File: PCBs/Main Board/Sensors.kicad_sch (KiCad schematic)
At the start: 3 parts, among them J6 436500301, J7 436500301, J8 43650-0401

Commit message: Remove steppers, add OLED
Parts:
- renumbered J6 to J7, J7 to J8, J8 to J9
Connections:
- net pH_rx renamed SCL
- net pH_tx renamed SDA
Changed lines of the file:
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@@
     )
   )
-  (global_label "pH_tx" (shape input) (at 135.89 76.2 0) (fields_autoplaced)
+  (global_label "SDA" (shape input) (at 135.89 76.2 0) (fields_autoplaced)
     (effects (font (size 1.27 1.27)) (justify left))
-    (property "Intersheet References" "${INTERSHEET_REFS}" (id 0) (at 143.5041 76.1206 0)
+    (property "Intersheet References" "${INTERSHEET_REFS}" (id 0) (at 141.8712 76.1206 0)
       (effects (font (size 1.27 1.27)) (justify left) hide)
     )
@@
     )
   )
-  (global_label "pH_rx" (shape input) (at 135.89 80.01 0) (fields_autoplaced)
+  (global_label "SCL" (shape input) (at 135.89 80.01 0) (fields_autoplaced)
     (effects (font (size 1.27 1.27)) (justify left))
-    (property "Intersheet References" "${INTERSHEET_REFS}" (id 0) (at 143.5645 79.9306 0)
+    (property "Intersheet References" "${INTERSHEET_REFS}" (id 0) (at 141.8107 79.9306 0)
       (effects (font (size 1.27 1.27)) (justify left) hide)
     )
@@
   (symbol (lib_id "power:GND") (at 133.35 62.23 0) (unit 1)
     (in_bom yes) (on_board yes) (fields_autoplaced)
-    (property "Reference" "#PWR011" (id 0) (at 133.35 68.58 0)
+    (property "Reference" "#PWR019" (id 0) (at 133.35 68.58 0)
       (effects (font (size 1.27 1.27)) hide)
     )
@@
   (symbol (lib_id "power:GND") (at 104.14 67.31 0) (unit 1)
     (in_bom yes) (on_board yes) (fields_autoplaced)
-    (property "Reference" "#PWR010" (id 0) (at 104.14 73.66 0)
+    (property "Reference" "#PWR018" (id 0) (at 104.14 73.66 0)
       (effects (font (size 1.27 1.27)) hide)
     )
@@
   (symbol (lib_id "power:GND") (at 55.88 90.17 0) (unit 1)
     (in_bom yes) (on_board yes) (fields_autoplaced)
-    (property "Reference" "#PWR09" (id 0) (at 55.88 96.52 0)
+    (property "Reference" "#PWR017" (id 0) (at 55.88 96.52 0)
       (effects (font (size 1.27 1.27)) hide)
     )
@@
   (symbol (lib_id "43650-0401:43650-0401") (at 130.81 52.07 90) (unit 1)
     (in_bom yes) (on_board yes) (fields_autoplaced)
-    (property "Reference" "J8" (id 0) (at 139.7 50.7999 90)
+    (property "Reference" "J9" (id 0) (at 139.7 50.7999 90)
       (effects (font (size 1.27 1.27)) (justify right))
     )
@@
   (symbol (lib_id "436500301:436500301") (at 73.66 54.61 90) (unit 1)
     (in_bom yes) (on_board yes) (fields_autoplaced)
-    (property "Reference" "J6" (id 0) (at 80.01 49.5299 90)
+    (property "Reference" "J7" (id 0) (at 80.01 49.5299 90)
       (effects (font (size 1.27 1.27)) (justify right))
     )
@@
   (symbol (lib_id "436500301:436500301") (at 101.6 54.61 90) (unit 1)
     (in_bom yes) (on_board yes) (fields_autoplaced)
-    (property "Reference" "J7" (id 0) (at 107.95 49.5299 90)
+    (property "Reference" "J8" (id 0) (at 107.95 49.5299 90)
       (effects (font (size 1.27 1.27)) (justify right))
     )

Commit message: Changed some pins
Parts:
- added J11: 436500301, SnapEDA Library:MOLEX_436500301, symbol 436500301:436500301
- renumbered J9 to J10, J7 to J8, J8 to J9
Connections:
- net 3V3: now also J11.1
- new net waterLevel: J11.3
- no-connect marks 0 -> 1
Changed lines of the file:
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@@
 (kicad_sch (version 20211123) (generator eeschema)
   (paper "A4")
+  (no_connect (at 162.56 59.69))
   (wire (pts (xy 128.27 80.01) (xy 135.89 80.01))
     (stroke (width 0) (type default) (color 0 0 0 0))
@@
     (stroke (width 0) (type default) (color 0 0 0 0))
   )
+  (wire (pts (xy 165.1 62.23) (xy 165.1 59.69))
+    (stroke (width 0) (type default) (color 0 0 0 0))
+  )
   (wire (pts (xy 73.66 59.69) (xy 73.66 85.09))
     (stroke (width 0) (type default) (color 0 0 0 0))
@@
     (stroke (width 0) (type default) (color 0 0 0 0))
   )
+  (wire (pts (xy 160.02 66.04) (xy 160.02 59.69))
+    (stroke (width 0) (type default) (color 0 0 0 0))
+  )
   (wire (pts (xy 130.81 62.23) (xy 130.81 76.2))
     (stroke (width 0) (type default) (color 0 0 0 0))
@@
     (stroke (width 0) (type default) (color 0 0 0 0))
   )
+  (global_label "waterLevel" (shape input) (at 165.1 62.23 0) (fields_autoplaced)
+    (effects (font (size 1.27 1.27)) (justify left))
+    (property "Intersheet References" "${INTERSHEET_REFS}" (id 0) (at 177.4312 62.1506 0)
+      (effects (font (size 1.27 1.27)) (justify left) hide)
+    )
+  )
+  (global_label "3V3" (shape input) (at 160.02 66.04 0) (fields_autoplaced)
+    (effects (font (size 1.27 1.27)) (justify left))
+    (property "Intersheet References" "${INTERSHEET_REFS}" (id 0) (at 165.9407 65.9606 0)
+      (effects (font (size 1.27 1.27)) (justify left) hide)
+    )
+  )
   (global_label "ec_A" (shape input) (at 55.88 80.01 180) (fields_autoplaced)
     (effects (font (size 1.27 1.27)) (justify right))
@@
   (symbol (lib_id "power:GND") (at 133.35 62.23 0) (unit 1)
     (in_bom yes) (on_board yes) (fields_autoplaced)
-    (property "Reference" "#PWR019" (id 0) (at 133.35 68.58 0)
+    (property "Reference" "#PWR022" (id 0) (at 133.35 68.58 0)
       (effects (font (size 1.27 1.27)) hide)
     )
@@
   (symbol (lib_id "power:GND") (at 104.14 67.31 0) (unit 1)
     (in_bom yes) (on_board yes) (fields_autoplaced)
-    (property "Reference" "#PWR018" (id 0) (at 104.14 73.66 0)
+    (property "Reference" "#PWR021" (id 0) (at 104.14 73.66 0)
       (effects (font (size 1.27 1.27)) hide)
     )
@@
     (pin "1")
   )
+  (symbol (lib_id "436500301:436500301") (at 162.56 54.61 90) (unit 1)
+    (in_bom yes) (on_board yes) (fields_autoplaced)
+    (property "Reference" "J11" (id 0) (at 168.91 49.5299 90)
+      (effects (font (size 1.27 1.27)) (justify right))
+    )
+    (property "Value" "436500301" (id 1) (at 168.91 52.0699 90)
+      (effects (font (size 1.27 1.27)) (justify right))
+    )
+    (property "Footprint" "SnapEDA Library:MOLEX_436500301" (id 2) (at 162.56 54.61 0)
+      (effects (font (size 1.27 1.27)) (justify left bottom) hide)
+    )
+    (property "Datasheet" "" (id 3) (at 162.56 54.61 0)
+      (effects (font (size 1.27 1.27)) (justify left bottom) hide)
+    )
+    (property "MAXIMUM_PACKAGE_HEIGHT" "5.57 mm" (id 4) (at 162.56 54.61 0)
+      (effects (font (size 1.27 1.27)) (justify left bottom) hide)
+    )
+    (property "PARTREV" "D7" (id 5) (at 162.56 54.61 0)
+      (effects (font (size 1.27 1.27)) (justify left bottom) hide)
+    )
+    (property "MANUFACTURER" "Molex" (id 6) (at 162.56 54.61 0)
+      (effects (font (size 1.27 1.27)) (justify left bottom) hide)
+    )
+    (property "STANDARD" "Manufacturer Recommendations" (id 7) (at 162.56 54.61 0)
+      (effects (font (size 1.27 1.27)) (justify left bottom) hide)
+    )
+    (pin "1")
+    (pin "2")
+    (pin "3")
+  )
   (symbol (lib_id "power:GND") (at 55.88 90.17 0) (unit 1)
     (in_bom yes) (on_board yes) (fields_autoplaced)
-    (property "Reference" "#PWR017" (id 0) (at 55.88 96.52 0)
+    (property "Reference" "#PWR020" (id 0) (at 55.88 96.52 0)
       (effects (font (size 1.27 1.27)) hide)
     )
@@
   (symbol (lib_id "43650-0401:43650-0401") (at 130.81 52.07 90) (unit 1)
     (in_bom yes) (on_board yes) (fields_autoplaced)
-    (property "Reference" "J9" (id 0) (at 139.7 50.7999 90)
+    (property "Reference" "J10" (id 0) (at 139.7 50.7999 90)
       (effects (font (size 1.27 1.27)) (justify right))
     )
@@
   (symbol (lib_id "436500301:436500301") (at 73.66 54.61 90) (unit 1)
     (in_bom yes) (on_board yes) (fields_autoplaced)
-    (property "Reference" "J7" (id 0) (at 80.01 49.5299 90)
+    (property "Reference" "J8" (id 0) (at 80.01 49.5299 90)
       (effects (font (size 1.27 1.27)) (justify right))
     )
@@
   (symbol (lib_id "436500301:436500301") (at 101.6 54.61 90) (unit 1)
     (in_bom yes) (on_board yes) (fields_autoplaced)
-    (property "Reference" "J8" (id 0) (at 107.95 49.5299 90)
-      (effects (font (size 1.27 1.27)) (justify right))
-    )
+    (property "Reference" "J9" (id 0) (at 107.95 49.5299 90)
+      (effects (font (size 1.27 1.27)) (justify right))
+    )

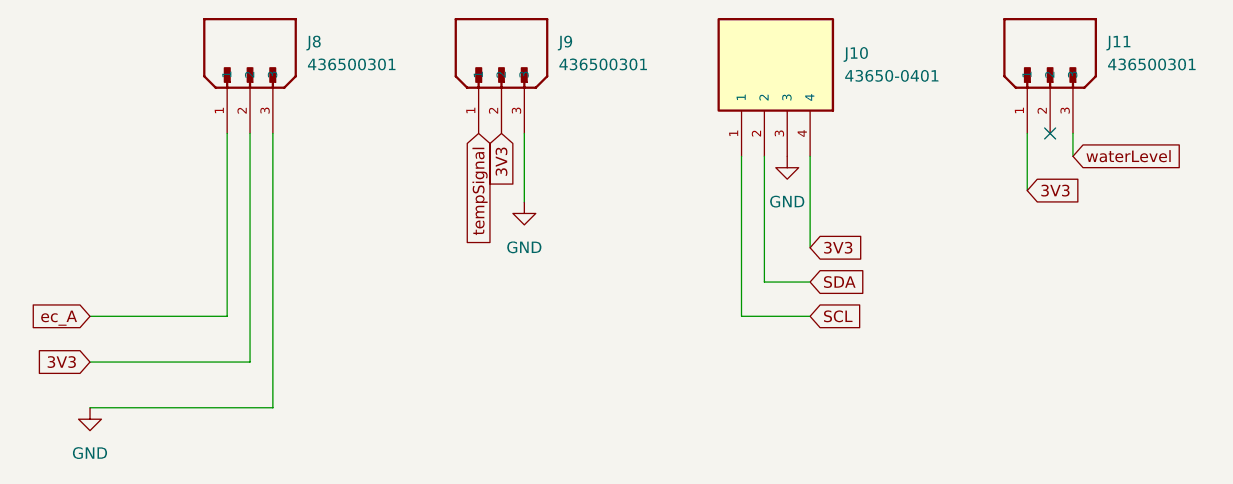
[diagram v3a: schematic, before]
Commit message: Changes to PCB, wired sensors to board
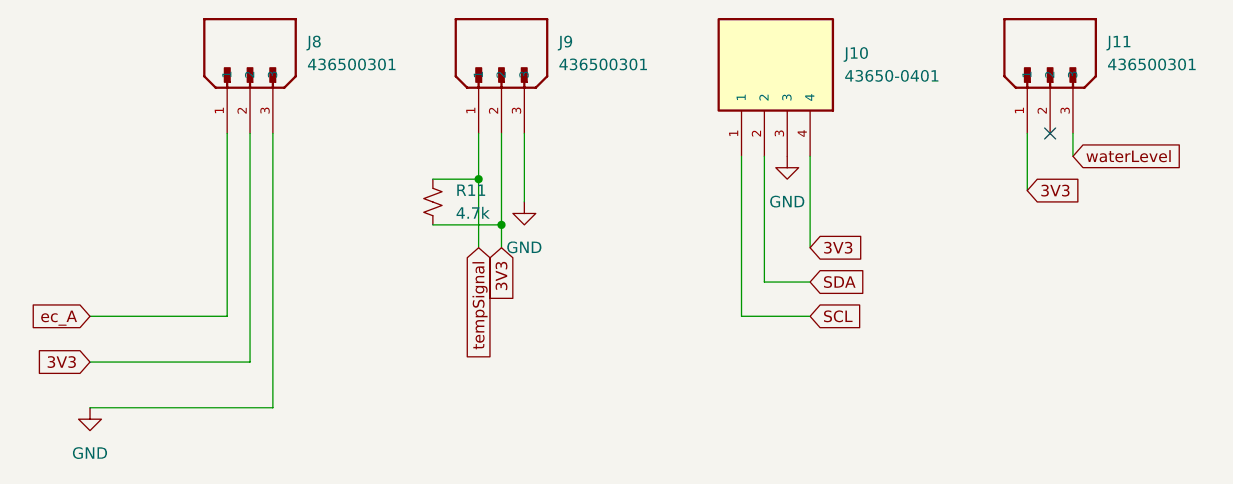
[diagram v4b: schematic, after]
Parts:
- added R11: 4.7k, Resistor_THT:R_Axial_DIN0204_L3.6mm_D1.6mm_P7.62mm_Horizontal, symbol Device:R_Small_US
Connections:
- net 3V3: now also R11.2
- net tempSignal: now also R11.1
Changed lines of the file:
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@@
 (kicad_sch (version 20211123) (generator eeschema)
   (paper "A4")
+  (junction (at 101.6 69.85) (diameter 0) (color 0 0 0 0)
+  )
+  (junction (at 99.06 64.77) (diameter 0) (color 0 0 0 0)
+  )
   (no_connect (at 162.56 59.69))
   (wire (pts (xy 128.27 80.01) (xy 135.89 80.01))
@@
   )
   (wire (pts (xy 55.88 85.09) (xy 73.66 85.09))
+    (stroke (width 0) (type default) (color 0 0 0 0))
+  )
+  (wire (pts (xy 93.98 64.77) (xy 99.06 64.77))
     (stroke (width 0) (type default) (color 0 0 0 0))
   )
@@
     (stroke (width 0) (type default) (color 0 0 0 0))
   )
+  (wire (pts (xy 99.06 72.39) (xy 99.06 64.77))
+    (stroke (width 0) (type default) (color 0 0 0 0))
+  )
+  (wire (pts (xy 93.98 69.85) (xy 101.6 69.85))
+    (stroke (width 0) (type default) (color 0 0 0 0))
+  )
   (wire (pts (xy 130.81 62.23) (xy 130.81 76.2))
+    (stroke (width 0) (type default) (color 0 0 0 0))
+  )
+  (wire (pts (xy 99.06 64.77) (xy 99.06 59.69))
+    (stroke (width 0) (type default) (color 0 0 0 0))
+  )
+  (wire (pts (xy 101.6 72.39) (xy 101.6 69.85))
+    (stroke (width 0) (type default) (color 0 0 0 0))
+  )
+  (wire (pts (xy 101.6 69.85) (xy 101.6 59.69))
     (stroke (width 0) (type default) (color 0 0 0 0))
   )
@@
     )
   )
-  (global_label "3V3" (shape input) (at 101.6 59.69 270) (fields_autoplaced)
+  (global_label "3V3" (shape input) (at 101.6 72.39 270) (fields_autoplaced)
     (effects (font (size 1.27 1.27)) (justify right))
-    (property "Intersheet References" "${INTERSHEET_REFS}" (id 0) (at 101.5206 65.6107 90)
+    (property "Intersheet References" "${INTERSHEET_REFS}" (id 0) (at 101.5206 78.3107 90)
       (effects (font (size 1.27 1.27)) (justify right) hide)
     )
@@
     )
   )
-  (global_label "tempSignal" (shape input) (at 99.06 59.69 270) (fields_autoplaced)
+  (global_label "tempSignal" (shape input) (at 99.06 72.39 270) (fields_autoplaced)
     (effects (font (size 1.27 1.27)) (justify right))
-    (property "Intersheet References" "${INTERSHEET_REFS}" (id 0) (at 98.9806 72.6864 90)
+    (property "Intersheet References" "${INTERSHEET_REFS}" (id 0) (at 98.9806 85.3864 90)
       (effects (font (size 1.27 1.27)) (justify right) hide)
     )
@@
     )
   )
+  (symbol (lib_id "Device:R_Small_US") (at 93.98 67.31 0) (unit 1)
+    (in_bom yes) (on_board yes) (fields_autoplaced)
+    (property "Reference" "R11" (id 0) (at 96.52 66.0399 0)
+      (effects (font (size 1.27 1.27)) (justify left))
+    )
+    (property "Value" "4.7k" (id 1) (at 96.52 68.5799 0)
+      (effects (font (size 1.27 1.27)) (justify left))
+    )
+    (property "Footprint" "Resistor_THT:R_Axial_DIN0204_L3.6mm_D1.6mm_P7.62mm_Horizontal" (id 2) (at 93.98 67.31 0)
+      (effects (font (size 1.27 1.27)) hide)
+    )
+    (property "Datasheet" "~" (id 3) (at 93.98 67.31 0)
+      (effects (font (size 1.27 1.27)) hide)
+    )
+    (pin "1")
+    (pin "2")
+  )
   (symbol (lib_id "power:GND") (at 133.35 62.23 0) (unit 1)
